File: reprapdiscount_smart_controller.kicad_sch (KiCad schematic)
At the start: 48 parts, among them J1 USB_A, Q1 BC817, Q2 BC817, U1 74HC4050, U2 74HC4050, U3 Pico

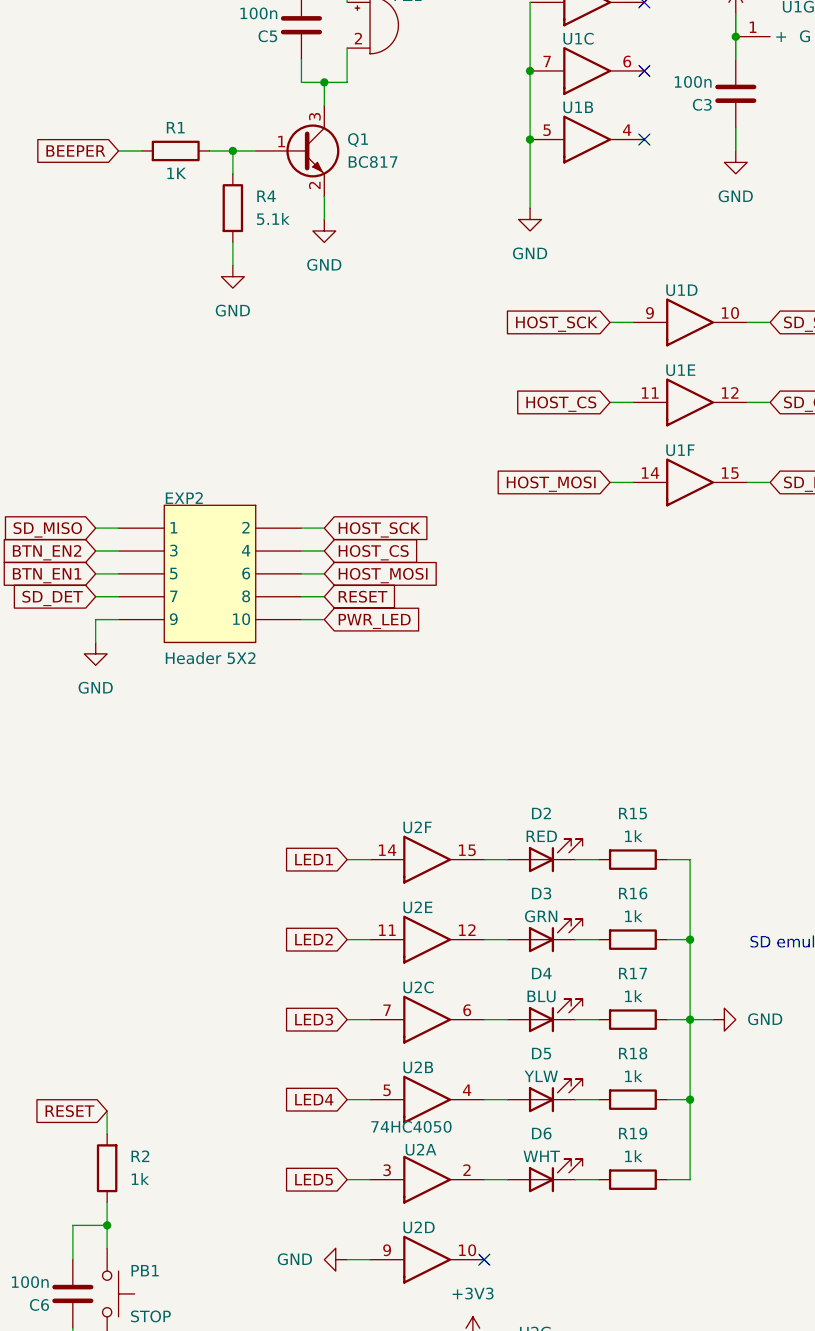
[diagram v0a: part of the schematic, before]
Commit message: bom: specify digikey part numbers
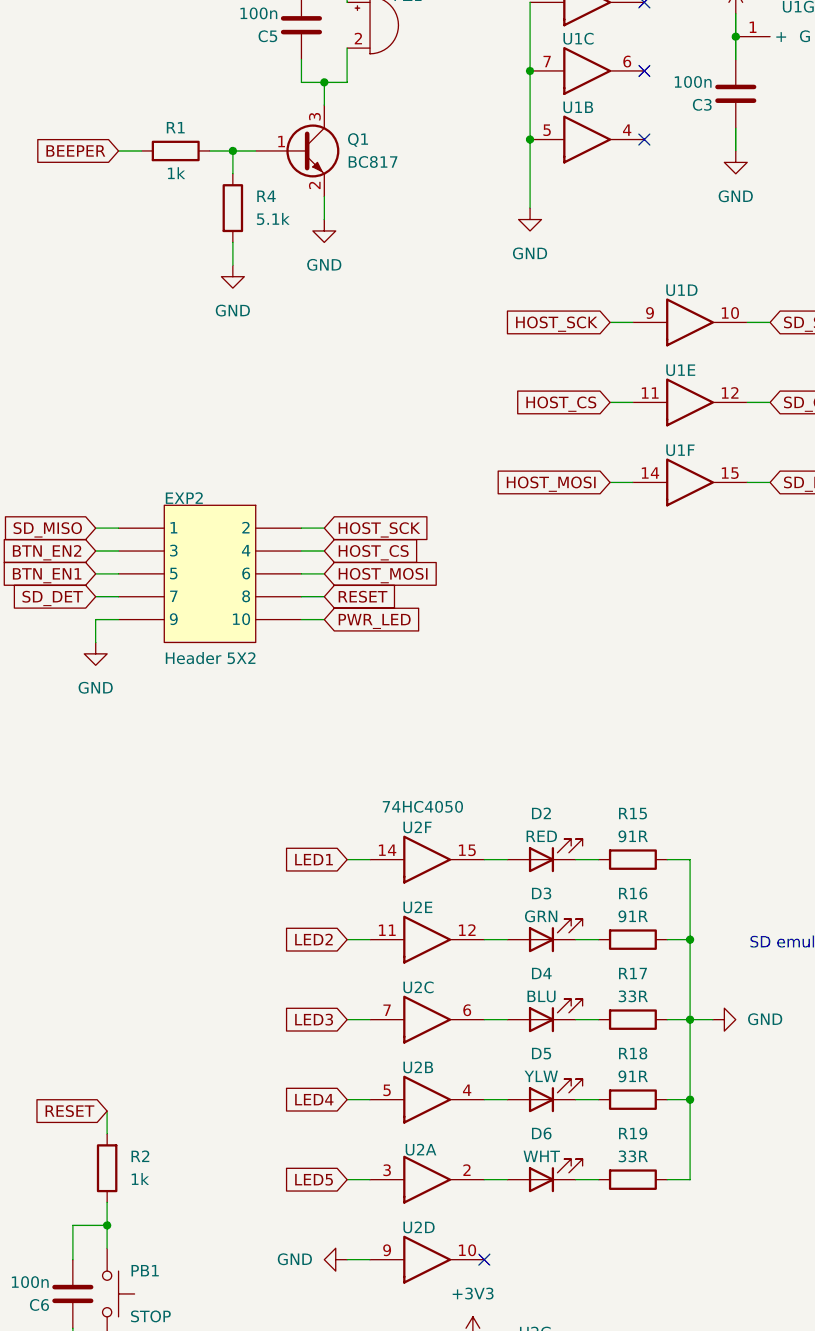
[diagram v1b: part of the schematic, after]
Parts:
- C1, C10, C4: ALTIUM_VALUE 100nF -> (none); Digikey (none) -> 1276-2399-1-ND; PUBLISHED 8-Jun-2000 -> (none); PUBLISHER Altium Limited -> (none); REVISION July-2002: Re-released for DXP Platform. -> (none)
- C2, C3, C5, C6, C7, C8, C9: ALTIUM_VALUE 100nF -> (none); Digikey (none) -> 478-KGM21NR71H104KMCT-ND; PUBLISHED 8-Jun-2000 -> (none); PUBLISHER Altium Limited -> (none); REVISION July-2002: Re-released for DXP Platform. -> (none)
- D1: Digikey (none) -> MBR120ESFT3GOSCT-ND
- D2: Digikey (none) -> 732-4984-1-ND
- D3: Digikey (none) -> 732-4986-1-ND
- D4: Digikey (none) -> 350-4394-1-ND
- D5: Digikey (none) -> 732-4987-1-ND
- D6: Digikey (none) -> 1516-QBLP631-IW5-2897CT-ND
- EN1: Digikey (none) -> PEC11R-4215K-S0024-ND
- EXP1, EXP2: Digikey (none) -> 1175-1627-ND; LATESTREVISIONDATE 17-Jul-2002 -> (none); LATESTREVISIONNOTE Re-released for DXP Platform. -> (none); PUBLISHER Altium Limited -> (none)
- J1: Digikey (none) -> 380-1412-ND
- PB1, PB2: Digikey (none) -> 2223-TS02-66-70-BK-160-LCR-D-ND
- PZ1: Digikey (none) -> 433-1028-ND
- Q1, Q2: COMPONENTLINK1DESCRIPTION Manufacturer Link -> (none); COMPONENTLINK1URL http://www.semiconductors.philips.com/ -> (none); COMPONENTLINK2DESCRIPTION Datasheet -> (none); COMPONENTLINK2URL http://www.semiconductors.philips.com/acrobat/datasheets/BC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 -> (none); DATASHEETVERSION 4-Feb-2002 -> (none); Digikey (none) -> BC817-25-TPMSCT-ND; LATESTREVISIONDATE 12-Dec-2006 -> (none); LATESTREVISIONNOTE IPC-7351 Footprint Added. -> (none); PACKAGEDESCRIPTION 3-Pin SOT-23 Package 0.95 mm Pitch, 2.3 mm Lead Span -> (none); PACKAGEREFERENCE SOT23 -> (none); PACKAGEVERSION May-1999 -> (none); PUBLISHED 17-Sep-2003 -> (none); PUBLISHER Altium Limited -> (none)
- R1: value 1K -> 1k; ALTIUM_VALUE 1K -> (none); Digikey (none) -> RNCP0805FTD1K00CT-ND; PUBLISHED 8-Jun-2000 -> (none); PUBLISHER Altium Limited -> (none); REVISION July-2002: Re-released for DXP Platform. -> (none)
- R10, R13: Digikey (none) -> 311-22ARCT-ND
- R12: Digikey (none) -> A130132CT-ND
- R14: Digikey (none) -> RMCF0805ZT0R00CT-ND
- R15, R16, R18: value 1k -> 91R; Digikey (none) -> 311-91.0CRCT-ND
- R17, R19: value 1k -> 33R; Digikey (none) -> 13-RC0805FR-1033RLCT-ND
- R2: Digikey (none) -> RNCP0805FTD1K00CT-ND
- R3, R9: Digikey (none) -> RC0805FR-07100RL
- R4, R5, R6: Digikey (none) -> 311-5.1KARCT-ND
- R7: Digikey (none) -> 118-TC33X-1-222ECT-ND
- R8: Digikey (none) -> 311-10KARCT-ND
- U1, U2: Digikey (none) -> 1727-6331-1-ND
- U3: Digikey (none) -> 2648-SC0915CT-ND

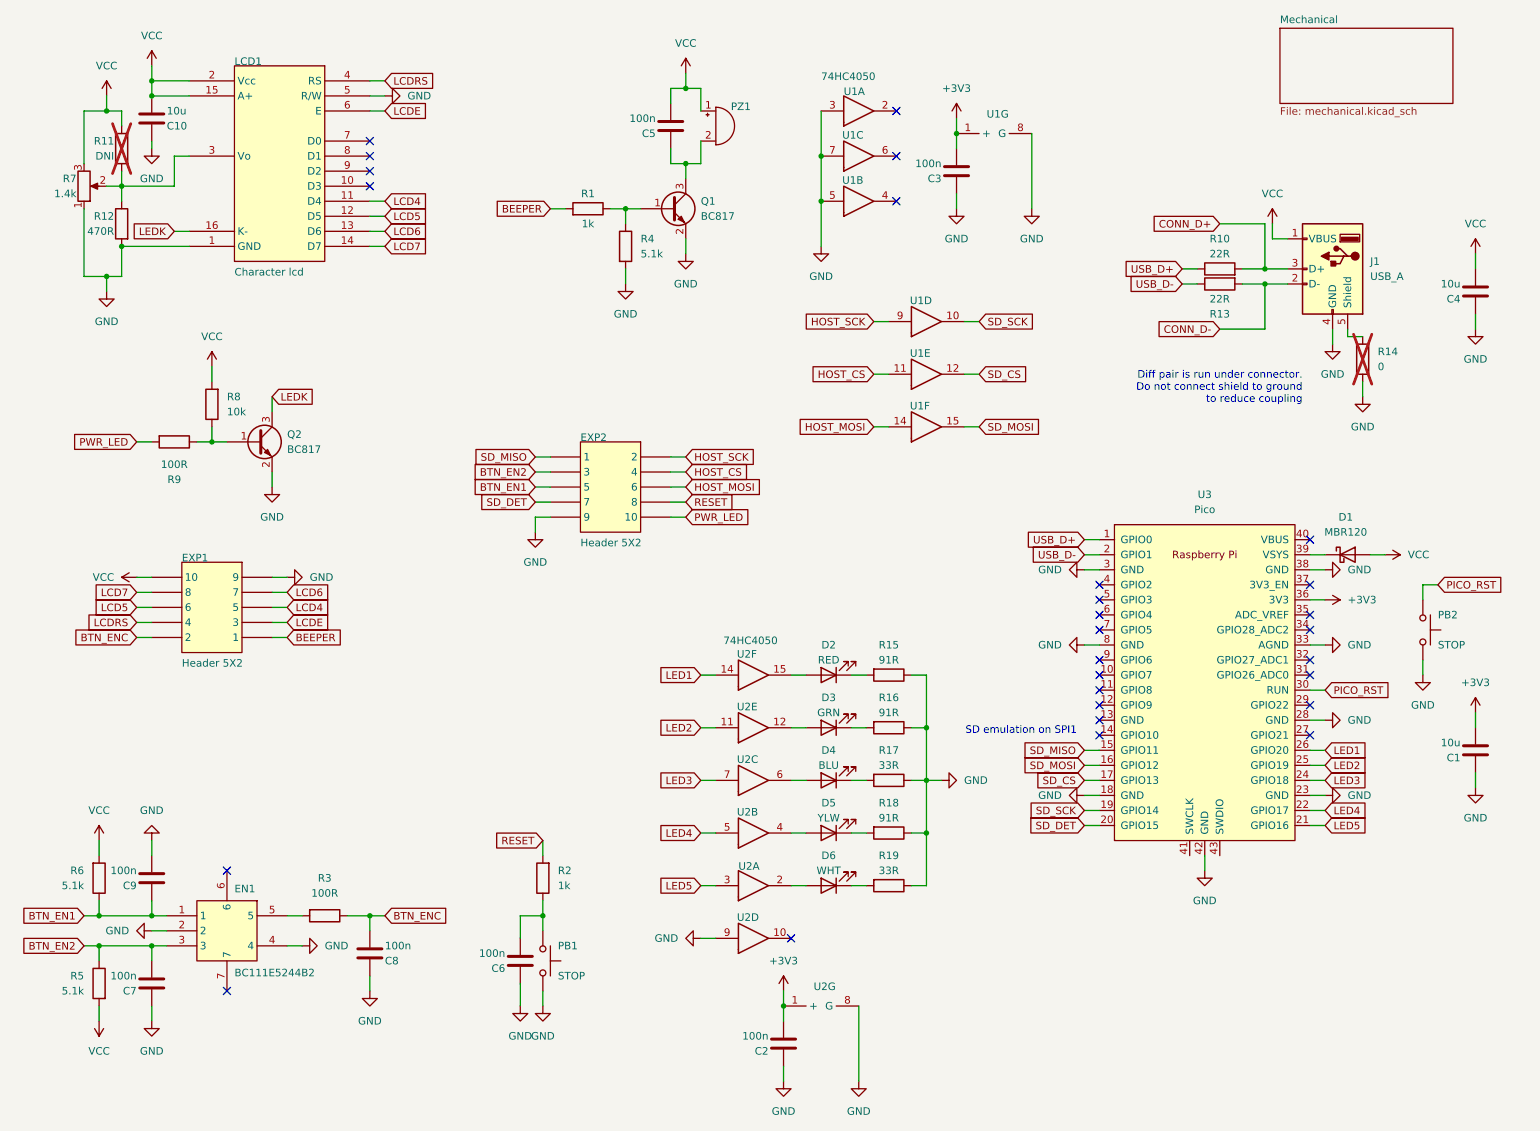
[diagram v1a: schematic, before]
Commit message: feature: support adafruit rgb display
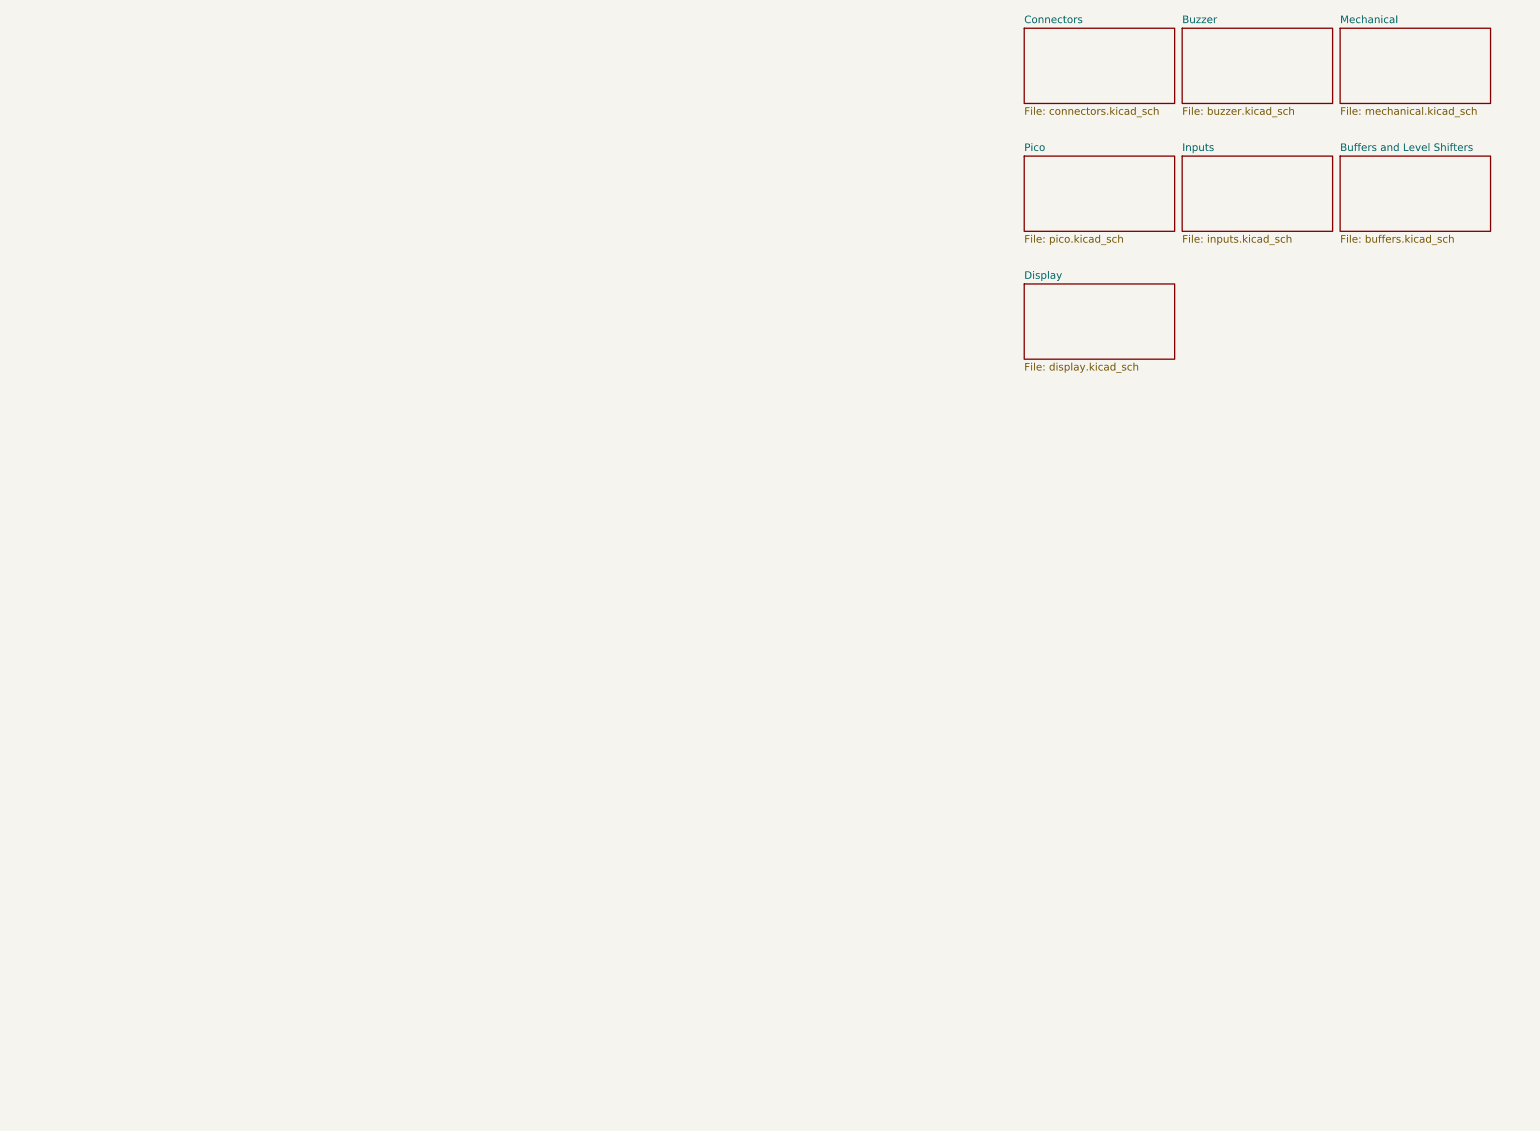
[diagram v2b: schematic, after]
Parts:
- removed C1, C10, C4: 10u, Capacitor_SMD:C_0805_2012Metric_Pad1.18x1.45mm_HandSolder, symbol Device:C
- removed C2, C3, C5, C6, C7, C8, C9: 100n, Capacitor_SMD:C_0805_2012Metric_Pad1.18x1.45mm_HandSolder, symbol Device:C
- removed D1: MBR120, Diode_SMD:D_SOD-123, symbol Device:D_Schottky
- removed D2: RED, LED_SMD:LED_0805_2012Metric_Pad1.15x1.40mm_HandSolder, symbol Device:LED
- removed D3: GRN, LED_SMD:LED_0805_2012Metric_Pad1.15x1.40mm_HandSolder, symbol Device:LED
- removed D4: BLU, LED_SMD:LED_0805_2012Metric_Pad1.15x1.40mm_HandSolder, symbol Device:LED
- removed D5: YLW, LED_SMD:LED_0805_2012Metric_Pad1.15x1.40mm_HandSolder, symbol Device:LED
- removed D6: WHT, LED_SMD:LED_0805_2012Metric_Pad1.15x1.40mm_HandSolder, symbol Device:LED
- removed EN1: BC111E5244B2, reprapdiscount_smart_controller:ROTARY ENCODER, symbol reprapdiscount_smart_controller-altium-import:root_0_Encoder
- removed EXP1: Header 5X2, reprapdiscount_smart_controller:HDR2X5_EXP, symbol reprapdiscount_smart_controller-altium-import:root_2_Header 5X2
- removed EXP2: Header 5X2, reprapdiscount_smart_controller:HDR2X5_EXP, symbol reprapdiscount_smart_controller-altium-import:root_0_Header 5X2
- removed J1: USB_A, Gigahawk:USB_A_Stewart_SS-52100-001_Horizontal, symbol Connector:USB_A
- removed LCD1: Character lcd, reprapdiscount_smart_controller:HDR1X16, symbol reprapdiscount_smart_controller-altium-import:root_0_mirrored_LCD characther
- removed PB1, PB2: STOP, Button_Switch_THT:SW_PUSH_6mm_H7.3mm, symbol Switch:SW_Push
- removed PZ1: PIEZO, reprapdiscount_smart_controller:PIEZO 11MM, symbol Device:Buzzer
- removed Q1, Q2: BC817, Package_TO_SOT_SMD:SOT-23, symbol Transistor_BJT:BC817
- removed R1, R2: 1k, Resistor_SMD:R_0805_2012Metric_Pad1.20x1.40mm_HandSolder, symbol Device:R
- removed R10, R13: 22R, Resistor_SMD:R_0805_2012Metric_Pad1.20x1.40mm_HandSolder, symbol Device:R
- removed R11: DNI, Resistor_SMD:R_0805_2012Metric_Pad1.20x1.40mm_HandSolder, symbol Device:R
- removed R12: 470R, Resistor_SMD:R_0805_2012Metric_Pad1.20x1.40mm_HandSolder, symbol Device:R
- removed R14: 0, Resistor_SMD:R_0805_2012Metric_Pad1.20x1.40mm_HandSolder, symbol Device:R
- removed R15, R16, R18: 91R, Resistor_SMD:R_0805_2012Metric_Pad1.20x1.40mm_HandSolder, symbol Device:R
- removed R17, R19: 33R, Resistor_SMD:R_0805_2012Metric_Pad1.20x1.40mm_HandSolder, symbol Device:R
- removed R3, R9: 100R, Resistor_SMD:R_0805_2012Metric_Pad1.20x1.40mm_HandSolder, symbol Device:R
- removed R4, R5, R6: 5.1k, Resistor_SMD:R_0805_2012Metric_Pad1.20x1.40mm_HandSolder, symbol Device:R
- removed R7: 1.4k, reprapdiscount_smart_controller:RES TRIMPOT, symbol Device:R_Potentiometer
- removed R8: 10k, Resistor_SMD:R_0805_2012Metric_Pad1.20x1.40mm_HandSolder, symbol Device:R
- removed U1, U2: 74HC4050, reprapdiscount_smart_controller:SO-16_3.9x9.9mm_P1.27mm, symbol reprapdiscount_smart_controller-altium-import:root_0_74HC4050
- removed U3: Pico, Gigahawk:RPi_Pico_SMD_NO_SILK, symbol gigahawk:Pico
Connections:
- no-connect marks 28 -> 0
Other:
- added sheet Buffers and Level Shifters (buffers.kicad_sch)
- added sheet Buzzer (buzzer.kicad_sch)
- added sheet Connectors (connectors.kicad_sch)
- added sheet Display (display.kicad_sch)
- added sheet Inputs (inputs.kicad_sch)
- added sheet Pico (pico.kicad_sch)
- note removed: "Diff pair is run under connector. Do not connect shield to ground to reduce coupling"
- note removed: "SD emulation on SPI1"
